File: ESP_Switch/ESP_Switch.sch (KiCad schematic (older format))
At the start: 26 parts, among them J1 Boot, J2 PRGM, J3 IO, J5 Expansion, J6 EXP2, J7 0548190519, U1 ESP-12E, U2 AMS1117-3.3

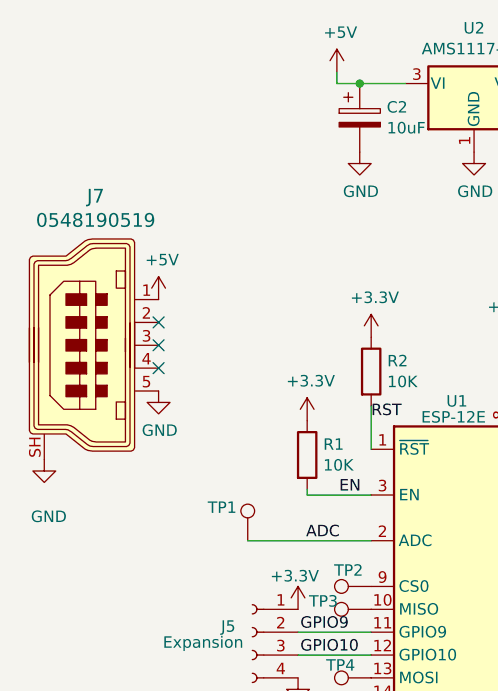
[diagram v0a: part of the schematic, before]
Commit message: added power distros
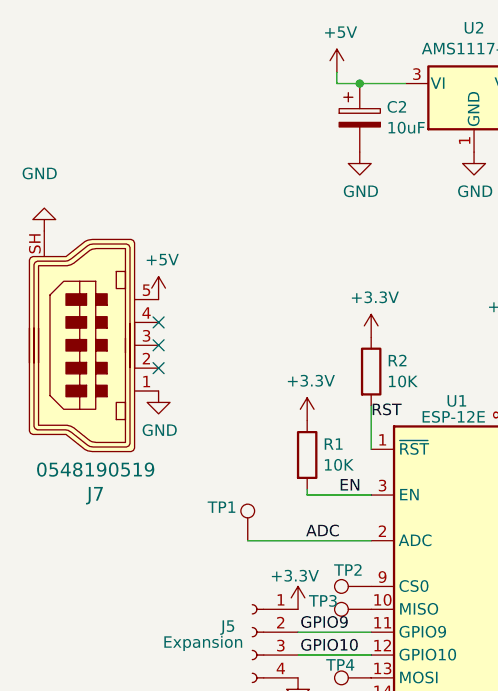
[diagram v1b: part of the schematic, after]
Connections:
- net +5V: now also J7.5; no longer J7.1
- net GND: now also J7.1; no longer J7.5
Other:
- moved on the sheet: J7
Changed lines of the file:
@@
 Sheet 1 1
 Title "ESP Switch"
-Date "2020-04-12"
-Rev "v1.1"
+Date "2020-06-10"
+Rev "v1.2"
 Comp ""
 Comment1 ""
@@
 L power:GND #PWR0102
 U 1 1 5E7459BA
-P 3420 3840
-F 0 "#PWR0102" H 3420 3590 50  0001 C CNN
-F 1 "GND" H 3440 3590 50  0000 C CNN
-F 2 "" H 3420 3840 50  0001 C CNN
-F 3 "" H 3420 3840 50  0001 C CNN
-	1    3420 3840
-	1    0    0    -1
+P 3420 2840
+F 0 "#PWR0102" H 3420 2590 50  0001 C CNN
+F 1 "GND" H 3440 2590 50  0000 C CNN
+F 2 "" H 3420 2840 50  0001 C CNN
+F 3 "" H 3420 2840 50  0001 C CNN
+	1    3420 2840
+	-1   0    0    1
 $EndComp
 $Comp
@@
 F 12 "Active" H 3820 4540 60  0001 L CNN "Status"
 	1    3620 3340
-	1    0    0    -1
-$EndComp
-Wire Wire Line
+	1    0    0    1
+$EndComp
+Wire Wire Line

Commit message: Added Pic and readme
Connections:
- net GND: now also J3.1 (Pin_1); no longer J3.2 (Pin_2)
- net GPIO13: now also J3.2 (Pin_2); no longer J3.1 (Pin_1)
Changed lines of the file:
@@
 L Connector:Screw_Terminal_01x02 J3
 U 1 1 5CC573E8
-P 6725 4495
-F 0 "J3" H 6805 4487 50  0000 L CNN
-F 1 "IO" H 6805 4396 50  0000 L CNN
-F 2 "TerminalBlock_Phoenix:TerminalBlock_Phoenix_MKDS-1,5-2_1x02_P5.00mm_Horizontal" H 6725 4495 50  0001 C CNN
-F 3 "~" H 6725 4495 50  0001 C CNN
-	1    6725 4495
-	1    0    0    -1
+P 6725 4595
+F 0 "J3" H 6805 4587 50  0000 L CNN
+F 1 "IO" H 6805 4496 50  0000 L CNN
+F 2 "TerminalBlock_Phoenix:TerminalBlock_Phoenix_MKDS-1,5-2_1x02_P5.00mm_Horizontal" H 6725 4595 50  0001 C CNN
+F 3 "~" H 6725 4595 50  0001 C CNN
+	1    6725 4595
+	1    0    0    1
 $EndComp
 Wire Wire Line
